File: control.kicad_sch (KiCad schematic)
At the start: 18 parts, among them J4 Conn_01x05_Pin, J5 Conn_01x03_Pin, J6 Conn_01x03_Pin, Q4 2N7002, U6 STM32G031G8Ux

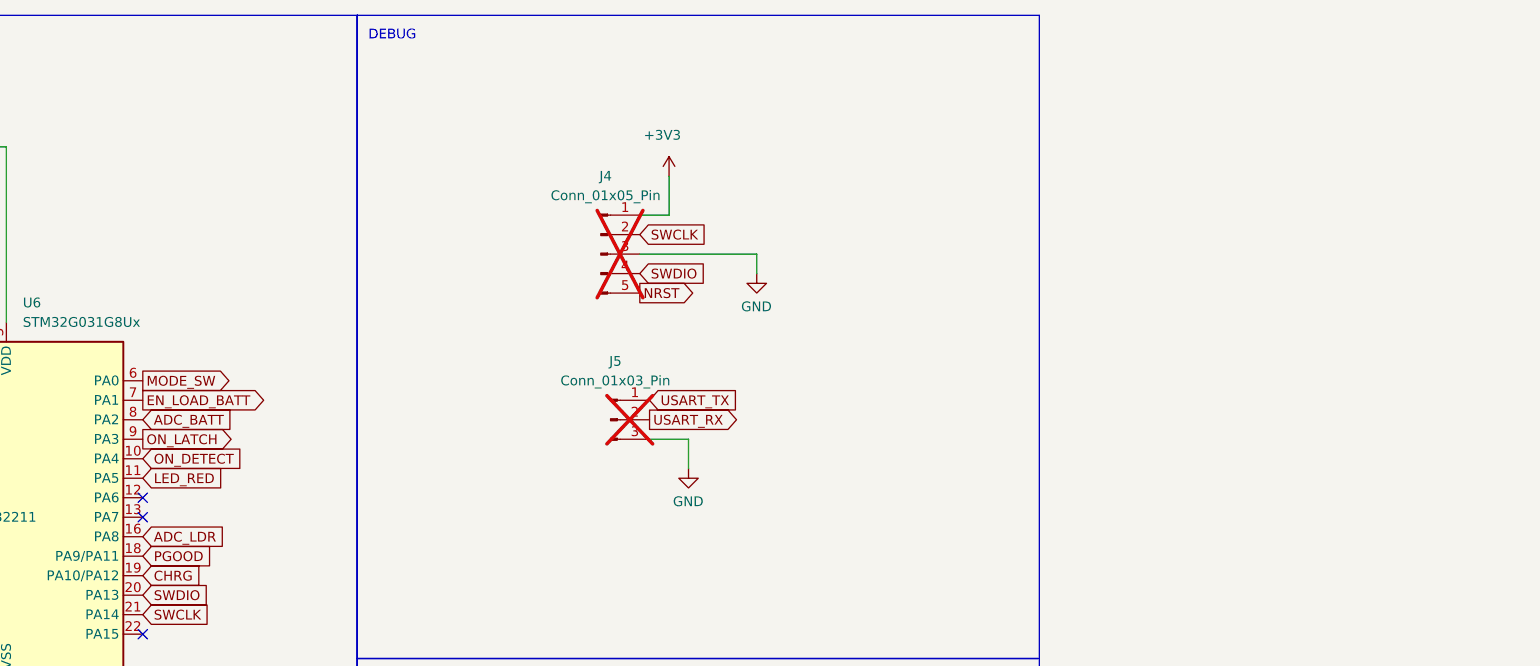
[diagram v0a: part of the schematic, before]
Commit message: v1 Revision - Better routing - Added testpoints - DUCK - Tweaked drawings
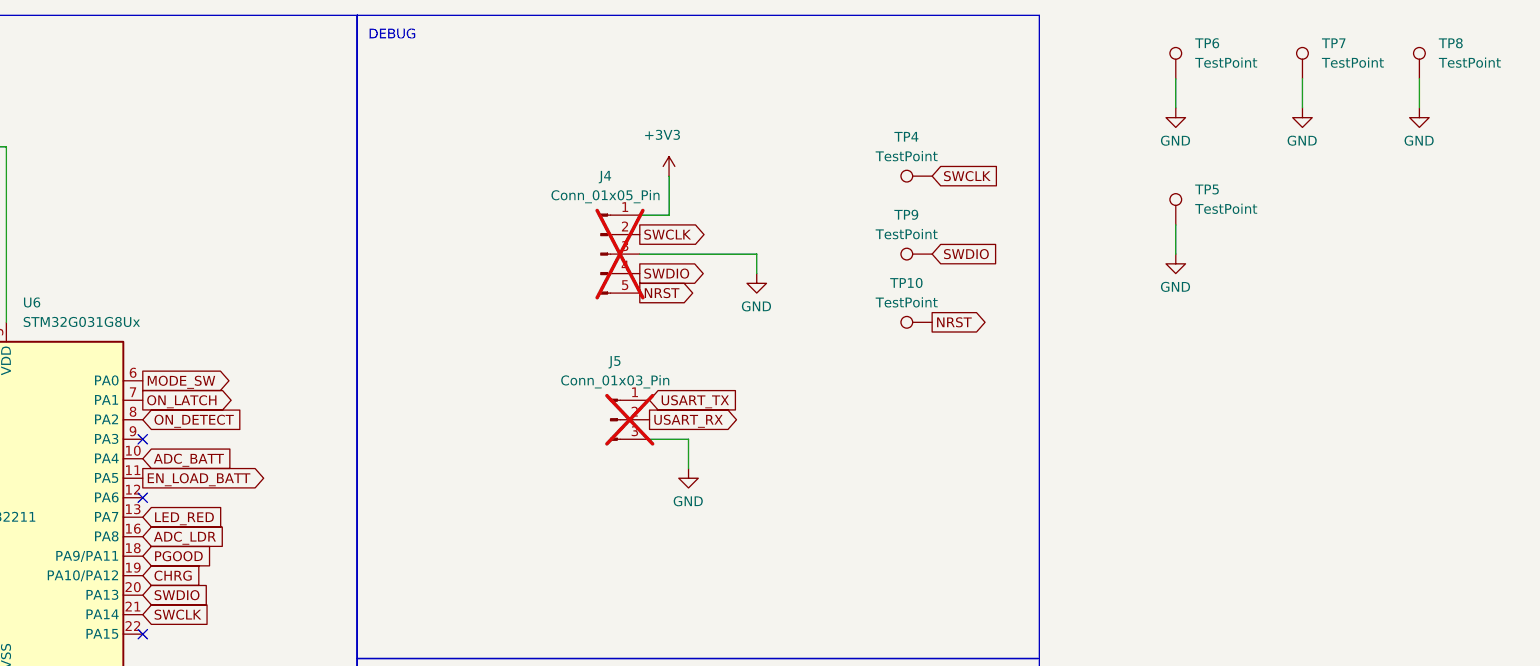
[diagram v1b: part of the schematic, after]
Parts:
- added TP10, TP4, TP5, TP7, TP8, TP9: TestPoint, TestPoint:TestPoint_Pad_D1.0mm, symbol Connector:TestPoint
- added TP6: TestPoint, TestPoint:TestPoint_Loop_D3.80mm_Drill2.0mm, symbol Connector:TestPoint
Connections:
- net ADC_BATT: now also U6.10 (PA4); no longer U6.8 (PA2)
- net EN_LOAD_BATT: now also U6.11 (PA5); no longer U6.7 (PA1)
- net GND: now also TP5.1, TP6.1, TP7.1, TP8.1
- net LED_RED: now also U6.13 (PA7); no longer U6.11 (PA5)
- net NRST: now also TP10.1
- net ON_DETECT: now also U6.8 (PA2); no longer U6.10 (PA4)
- net ON_LATCH: now also U6.7 (PA1); no longer U6.9 (PA3)
- net SWCLK: now also TP4.1
- net SWDIO: now also TP9.1

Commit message: v2 Rev
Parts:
- removed Q4: 2N7002, Package_TO_SOT_SMD:SOT-23, symbol Transistor_FET:2N7002
- removed R24: 100k, Resistor_SMD:R_0603_1608Metric, symbol Device:R
- added Q4: DTC143Z, SOT-523:SOT-523, symbol Transistor_BJT:DTC143Z
- R19: value 100k -> 10k
- R20, R21, R23: value 100 -> 220
- TP6: footprint TestPoint:TestPoint_Loop_D3.80mm_Drill2.0mm -> Connector_PinSocket_2.54mm:PinSocket_1x01_P2.54mm_Vertical
- renumbered TP5 to TP10, TP9 to TP4, TP10 to TP5, TP4 to TP9
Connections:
- net +3V3: now also Q4.3 (C)
- net ADC_LDR: now also U6.18 (PA9/PA11); no longer U6.16 (PA8)
- net CHRG: now also U6.14 (PB0); no longer U6.19 (PA10/PA12)
- net EN_LDR: now also U6.19 (PA10/PA12); no longer U6.15 (PB1)
- net EN_SERVO: now also U6.28 (PB8); no longer U6.25 (PB5)
- net PGOOD: now also U6.15 (PB1); no longer U6.18 (PA9/PA11)
- net SERWO_PWM: now also U6.25 (PB5); no longer U6.28 (PB8)
- net at J6.1 (Pin_1): now also Q4.2 (E)
- net at R22.2: now also Q4.1 (B)

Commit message: Made prettier look
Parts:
- TP6: footprint Connector_PinSocket_2.54mm:PinSocket_1x01_P2.54mm_Vertical -> Connector_PinHeader_2.54mm:PinHeader_1x01_P2.54mm_Vertical
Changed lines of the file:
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@@
 			)
 		)
-		(property "Footprint" "Connector_PinSocket_2.54mm:PinSocket_1x01_P2.54mm_Vertical"
+		(property "Footprint" "Connector_PinHeader_2.54mm:PinHeader_1x01_P2.54mm_Vertical"
 			(at 241.3 24.13 0)
 			(effects
